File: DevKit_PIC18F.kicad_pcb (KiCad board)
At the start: 2 copper layers, 25 parts, among them J1 PIC_ICSP_ICD, J2 USB_B, J4 RA_PORT, J5 RB_PORT, J6 RD_PORT, J7 RC_PORT, J8 RE_PORT, J9 2P_UART, SW1 SW_DIP, X1 16MHz

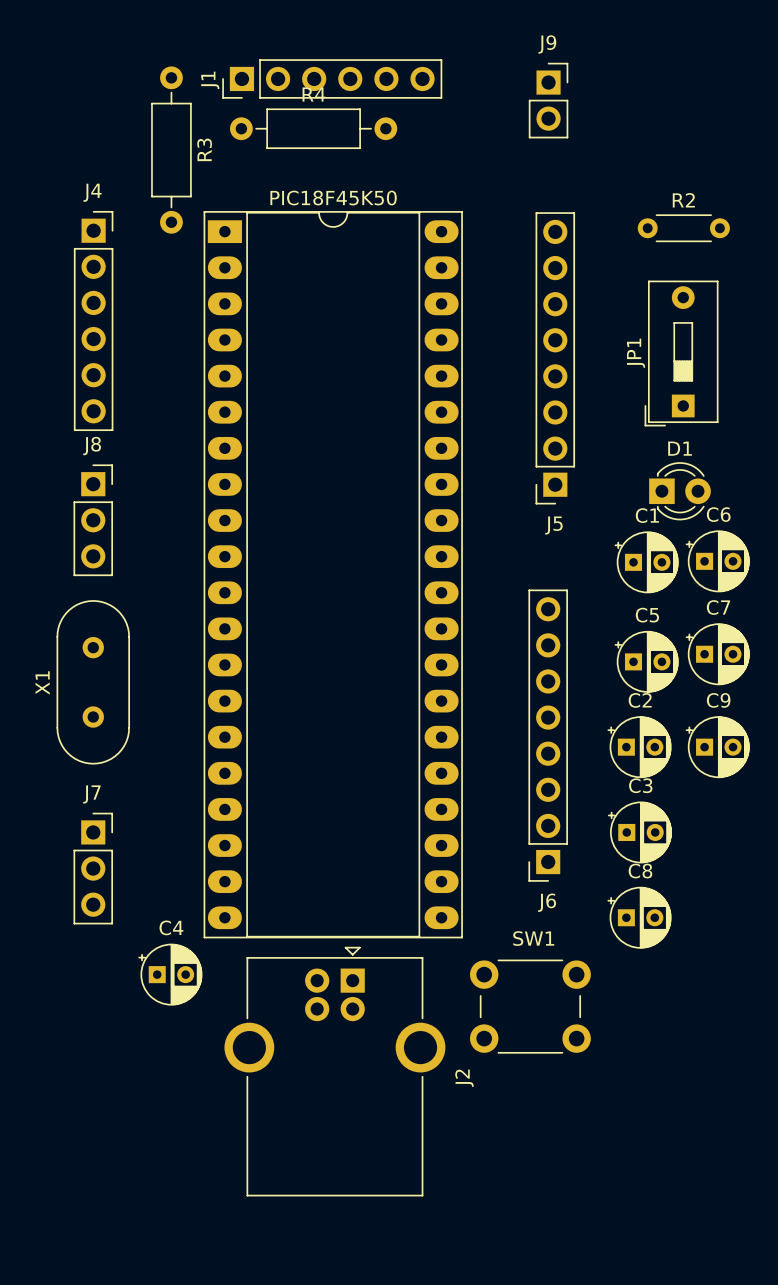
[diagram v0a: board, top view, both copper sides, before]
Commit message: Change USB-B -> USB-C & Added EdgeCut.
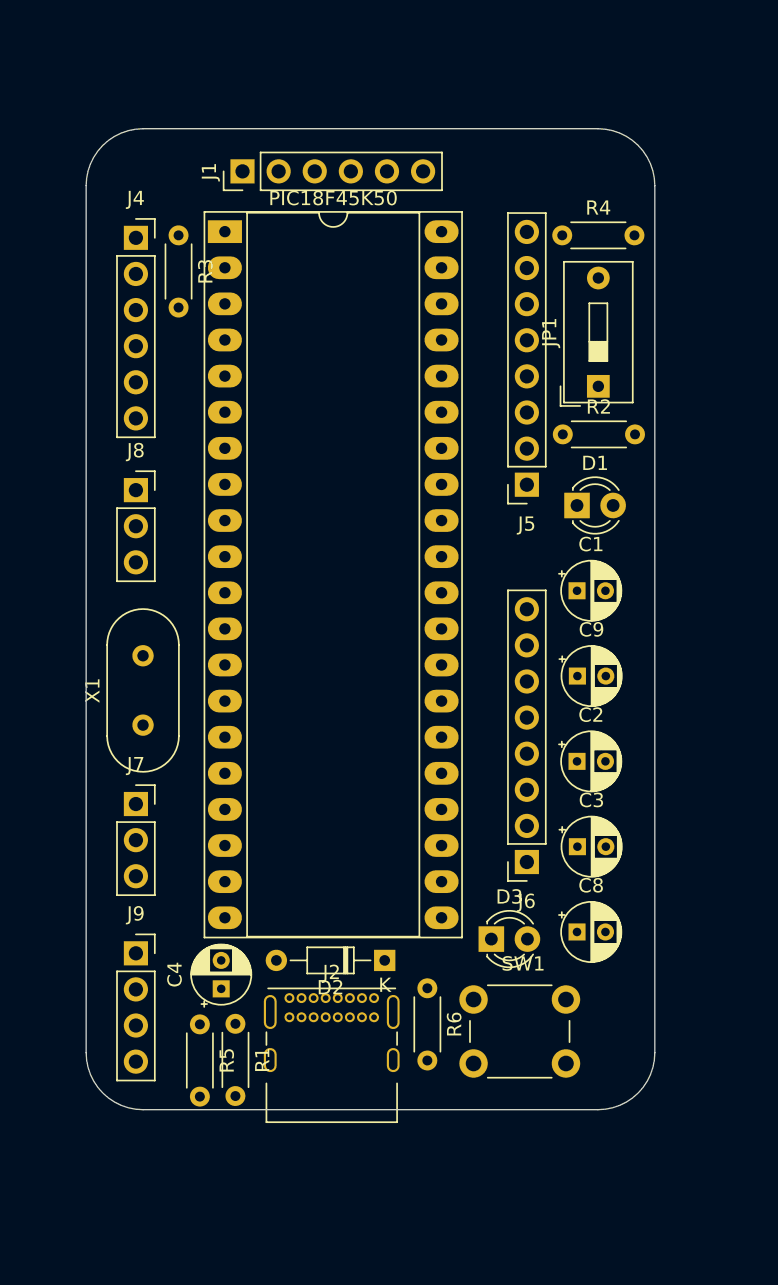
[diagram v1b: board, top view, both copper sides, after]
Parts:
- removed C5: 100nF, Capacitor_THT:CP_Radial_D4.0mm_P2.00mm
- removed C6, C7: 47uF, Capacitor_THT:CP_Radial_D4.0mm_P2.00mm
- added D2: D_Schottky, Diode_THT:D_DO-34_SOD68_P7.62mm_Horizontal, F.Cu at (89.0, 85.0)
- added D3: LED_PWR, LED_THT:LED_D3.0mm_FlatTop, F.Cu at (96.5, 83.5)
- added R1: 5.1k, Resistor_THT:R_Axial_DIN0204_L3.6mm_D1.6mm_P5.08mm_Horizontal, F.Cu at (78.5, 89.5)
- added R5: 5.1k, Resistor_THT:R_Axial_DIN0204_L3.6mm_D1.6mm_P5.08mm_Horizontal, F.Cu at (76.0, 89.5)
- added R6: 330, Resistor_THT:R_Axial_DIN0204_L3.6mm_D1.6mm_P5.08mm_Horizontal, F.Cu at (92.0, 87.0)
- D1: value LED -> LED_RST; footprint LED_THT:LED_D3.0mm -> LED_THT:LED_D3.0mm_FlatTop
- J2: value USB_B -> USB_C_Receptacle_USB2.0_16P; footprint Connector_USB:USB_B_OST_USB-B1HSxx_Horizontal -> Connector_USB:USB_C_Receptacle_GCT_USB4085
- J9: footprint Connector_PinSocket_2.54mm:PinSocket_1x02_P2.54mm_Vertical -> Connector_PinSocket_2.54mm:PinSocket_1x04_P2.54mm_Vertical
- R3, R4: footprint Resistor_THT:R_Axial_DIN0207_L6.3mm_D2.5mm_P10.16mm_Horizontal -> Resistor_THT:R_Axial_DIN0204_L3.6mm_D1.6mm_P5.08mm_Horizontal
- moved J9 67.8 mm to (71.5, 84.5)
- moved R4 23.8 mm to (101.5, 34.0)
- moved R2 15.7 mm to (101.5, 48.0)
- moved R3 11.1 mm to (74.5, 34.0)
- moved C9 10.2 mm to (102.6, 65.0)
- moved J1 6.50 mm to (79.0, 29.5)
- moved JP1 6.13 mm to (104.0, 44.6)
- moved D1 6.06 mm to (102.5, 53.0)
- moved J2 4.62 mm to (82.3, 87.7), turned to 0 degrees
- moved C4 4.61 mm to (77.5, 87.0), turned to 90 degrees
- moved C1 4.45 mm to (102.5, 59.0)
- moved C2 3.61 mm to (102.5, 71.0)
- moved C3 3.61 mm to (102.6, 77.0)
- moved C8 3.61 mm to (102.5, 83.0)
- moved J7 3.61 mm to (71.5, 74.0)
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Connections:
- C1 pad 2: VCC -> GND
- C3 pad 1: VCC -> GND
- C8 pad 1: VCC -> GND
- D1 pad 2: VCC -> GND
- J1 pad 2: VCC -> GND
- JP1 pad 2: VCC -> GND
- PIC18F45K50 pad 1: VCC -> GND
- PIC18F45K50 pad 11: VCC -> GND
- PIC18F45K50 pad 32: VCC -> GND
- R2 pad 2: VCC -> GND
- R3 pad 1: VCC -> GND
- R3 pad 2: VCC -> GND
- R4 pad 2: VCC -> GND
- SW1 pad 1: VCC -> GND
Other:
- board outline added: 40 x 69 mm

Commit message: Routed & Finished Rev.1
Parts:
- J9: footprint Connector_PinSocket_2.54mm:PinSocket_1x04_P2.54mm_Vertical -> Connector_PinSocket_2.54mm:PinSocket_1x05_P2.54mm_Vertical
- moved R3 31.5 mm to (102.0, 49.5), turned to 0 degrees
- moved J6 19.2 mm to (96.5, 59.0), turned to 0 degrees
- moved R5 18.5 mm to (94.5, 89.5)
- moved J5 17.7 mm to (96.5, 34.0), turned to 0 degrees
- moved JP1 15.4 mm to (105.0, 60.0)
- moved R4 13.0 mm to (102.0, 47.0)
- moved D1 11.0 mm to (103.2, 64.0)
- moved C1 10.0 mm to (103.0, 69.0)
- moved C9 9.01 mm to (103.0, 74.0)
- moved C2 8.02 mm to (103.0, 79.0)
- moved C3 7.02 mm to (103.0, 84.0)
- moved R2 6.53 mm to (107.0, 44.5), turned to 180 degrees
- moved D3 4.75 mm to (92.5, 86.0)
- moved C8 4.64 mm to (98.0, 84.0)
- moved J9 3.91 mm to (74.0, 81.5)
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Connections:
- J5 pad 7: /PGD -> /PGC
- J5 pad 8: /PGC -> /PGD
- J9 pad 4: GND -> unconnected-(J9-Pin_4-Pad4)
- PIC18F45K50 pad 39: /PGD -> /PGC
- PIC18F45K50 pad 40: /PGC -> /PGD
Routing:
- net GND: track 0.00 -> 220.5 mm, vias 0 -> 1
- net /PGD: track 0.00 -> 37.2 mm
- net /OSC2: track 0.00 -> 37.0 mm
- net Net-(J6-Pin_1): track 0.00 -> 33.5 mm
- net /MCLR: track 0.00 -> 33.5 mm
- net /OSC1: track 0.00 -> 33.1 mm
- net Net-(J6-Pin_3): track 0.00 -> 31.0 mm, vias 0 -> 3
- net Net-(J6-Pin_2): track 0.00 -> 29.2 mm
- net Net-(J9-Pin_1): track 0.00 -> 27.8 mm
- net Net-(J6-Pin_8): track 0.00 -> 26.2 mm
- net Net-(J6-Pin_7): track 0.00 -> 24.6 mm
- net Net-(J5-Pin_2): track 0.00 -> 24.3 mm
- net Net-(J9-Pin_2): track 0.00 -> 24.1 mm
- net /PGC: track 0.00 -> 22.8 mm
- net Net-(J5-Pin_1): track 0.00 -> 22.1 mm
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- added copper zone on B.Cu, net (none)
- added copper zone on F.Cu, net (none)
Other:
- board size 40 x 69 mm -> 41 x 71 mm
- board text added: "CTS"
- board text added: "GND"
- board text added: "ICSP"
- board text added: "PROG"
- board text added: "RA0"
- board text added: "RA1"
- board text added: "RA2"
- board text added: "RA3"
- board text added: "RA4"
- board text added: "RA5"
- board text added: "RB0/SDI/A"
- board text added: "RB1/SCK/L"
- board text added: "RB2"
- board text added: "RB3/SDO"
- board text added: "RB4"
- board text added: "RB5"
- board text added: "RB6"
- board text added: "RB7"
- board text added: "RC0"
- board text added: "RC1"
- board text added: "RC2"
- board text added: "RD0"
- board text added: "RD1"
- board text added: "RD2"
- board text added: "RD3"
- board text added: "RD4"
- board text added: "RD5"
- board text added: "RD6"
- board text added: "RD7"
- board text added: "RE0"
- board text added: "RE1"
- board text added: "RE2"
- board text added: "RESET"
- board text added: "RX"
- board text added: "TX"
- board text added: "UART"
- board text added: "VCC"

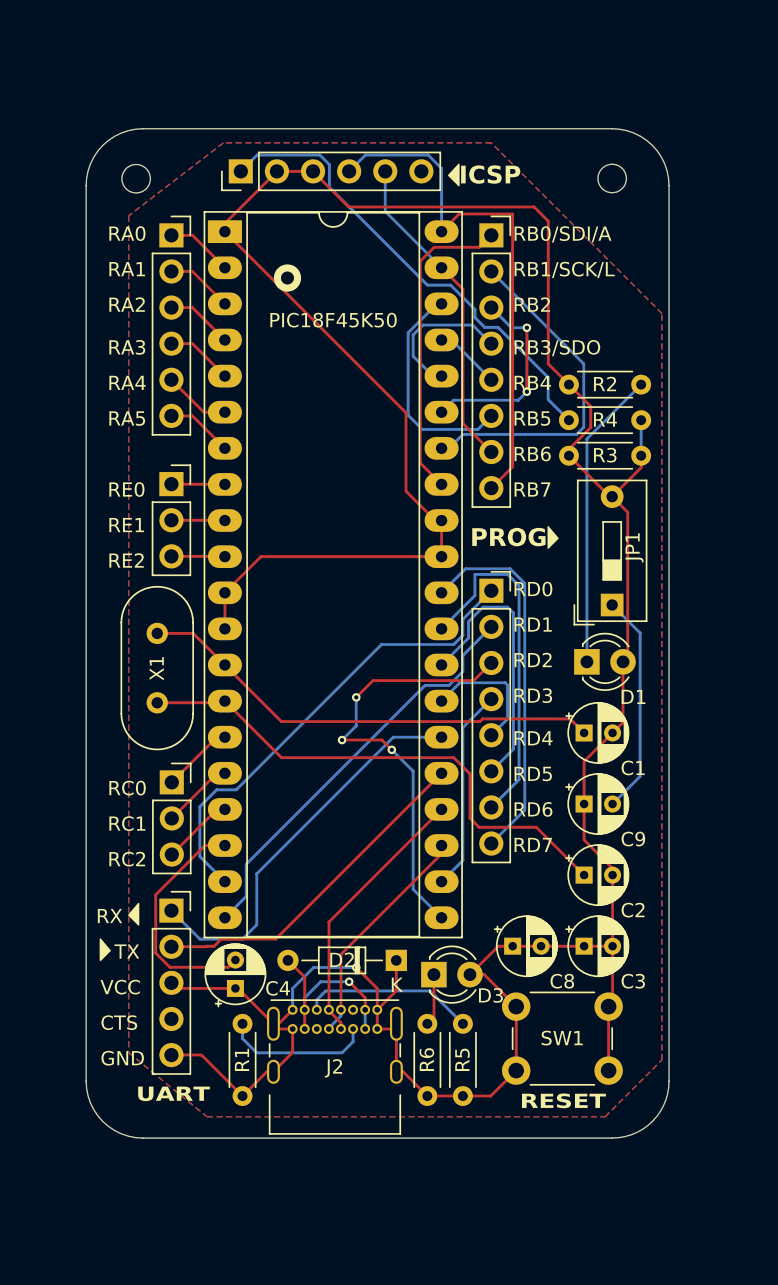
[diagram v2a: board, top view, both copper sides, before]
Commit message: Fixed Crystal Error & re-routed some more.
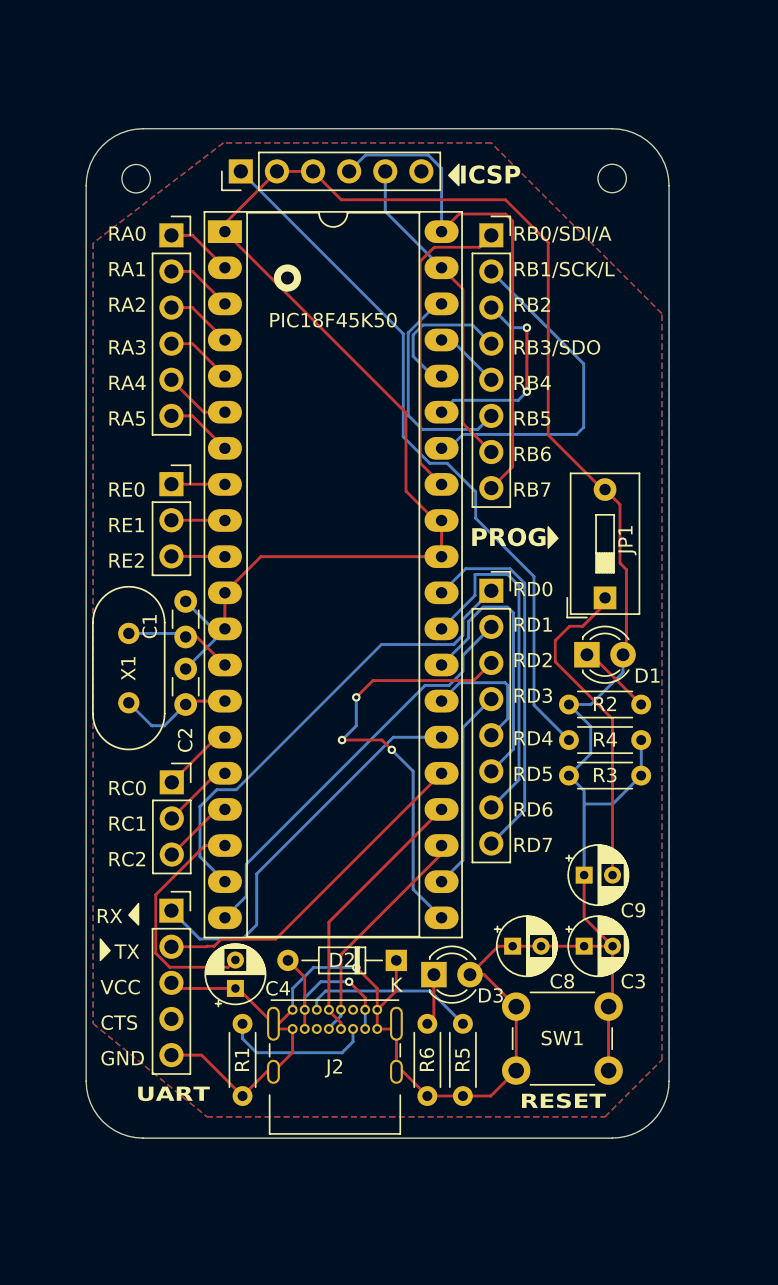
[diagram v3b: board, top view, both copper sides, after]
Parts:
- C1, C2: footprint Capacitor_THT:CP_Radial_D4.0mm_P2.00mm -> Capacitor_THT:C_Disc_D3.0mm_W1.6mm_P2.50mm
- moved C2 30.5 mm to (75.0, 67.0), turned to 90 degrees
- moved C1 28.8 mm to (75.0, 62.2), turned to 90 degrees
- moved R2 22.5 mm to (107.0, 67.0)
- moved R3 22.5 mm to (102.0, 72.0)
- moved R4 22.5 mm to (102.0, 69.5)
- moved C9 5.00 mm to (103.0, 79.0)
- moved X1 2.00 mm to (71.0, 66.9)
- moved JP1 0.71 mm to (104.5, 59.5)
- moved D1 0.50 mm to (103.2, 63.5)
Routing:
- net /OSC2: track 37.0 -> 8.32 mm
- net /OSC1: track 33.1 -> 7.68 mm
- net /MCLR: track 33.5 -> 50.3 mm
- net Net-(D1-K): track 21.1 -> 5.26 mm
- net GND: track 220.5 -> 230.6 mm
- net Net-(JP1-A): track 15.6 -> 23.2 mm

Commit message: refine routing
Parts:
- moved JP1 8.00 mm to (104.5, 67.5)
- moved D1 7.23 mm to (103.2, 56.3)
- moved R2 3.50 mm to (107.0, 70.5)
- moved R3 3.50 mm to (102.0, 75.5)
- moved R4 3.50 mm to (102.0, 73.0)
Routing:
- net Net-(JP1-A): track 23.2 -> 11.7 mm
- net Net-(D1-K): track 5.26 -> 15.8 mm
- net Net-(J6-Pin_3): track 31.0 -> 24.5 mm, vias 3 -> 1
- net Net-(J5-Pin_2): track 24.3 -> 18.0 mm
- net /MCLR: track 50.3 -> 54.6 mm
- net Net-(J6-Pin_1): track 33.5 -> 35.8 mm
- net Net-(J5-Pin_6): track 15.6 -> 17.8 mm
- net Net-(J5-Pin_3): track 14.2 -> 12.3 mm, vias 2 -> 0
- net /PGC: track 22.8 -> 24.1 mm
- net Net-(J6-Pin_8): track 26.2 -> 27.5 mm
- net /OSC2: track 8.32 -> 7.08 mm
- net Net-(J6-Pin_7): track 24.6 -> 25.7 mm
- net /PGD: track 36.9 -> 37.9 mm
- net Net-(PIC18F45K50-VUSB3V3): track 16.6 -> 17.2 mm
- net Net-(J5-Pin_1): track 22.1 -> 22.7 mm

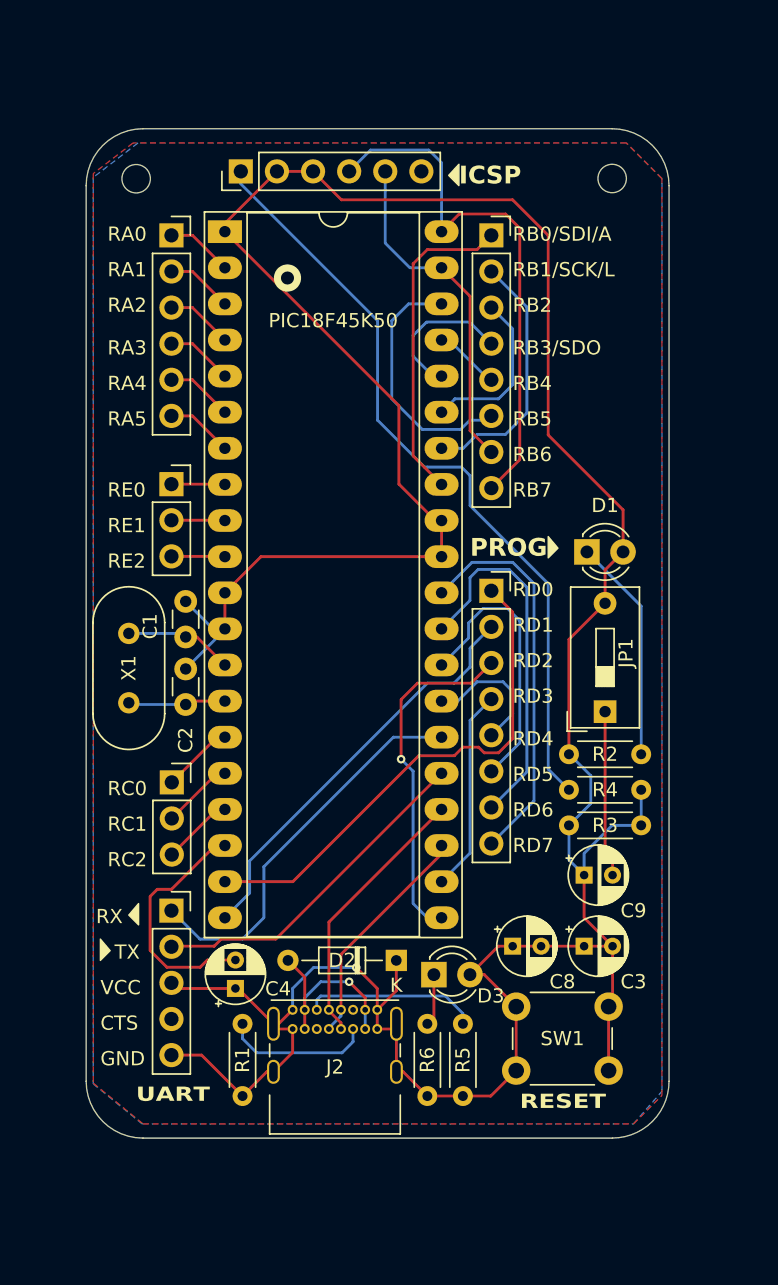
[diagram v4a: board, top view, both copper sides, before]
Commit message: Added ICSP LED, D+/- tuned length, Cap placement/footprint update.
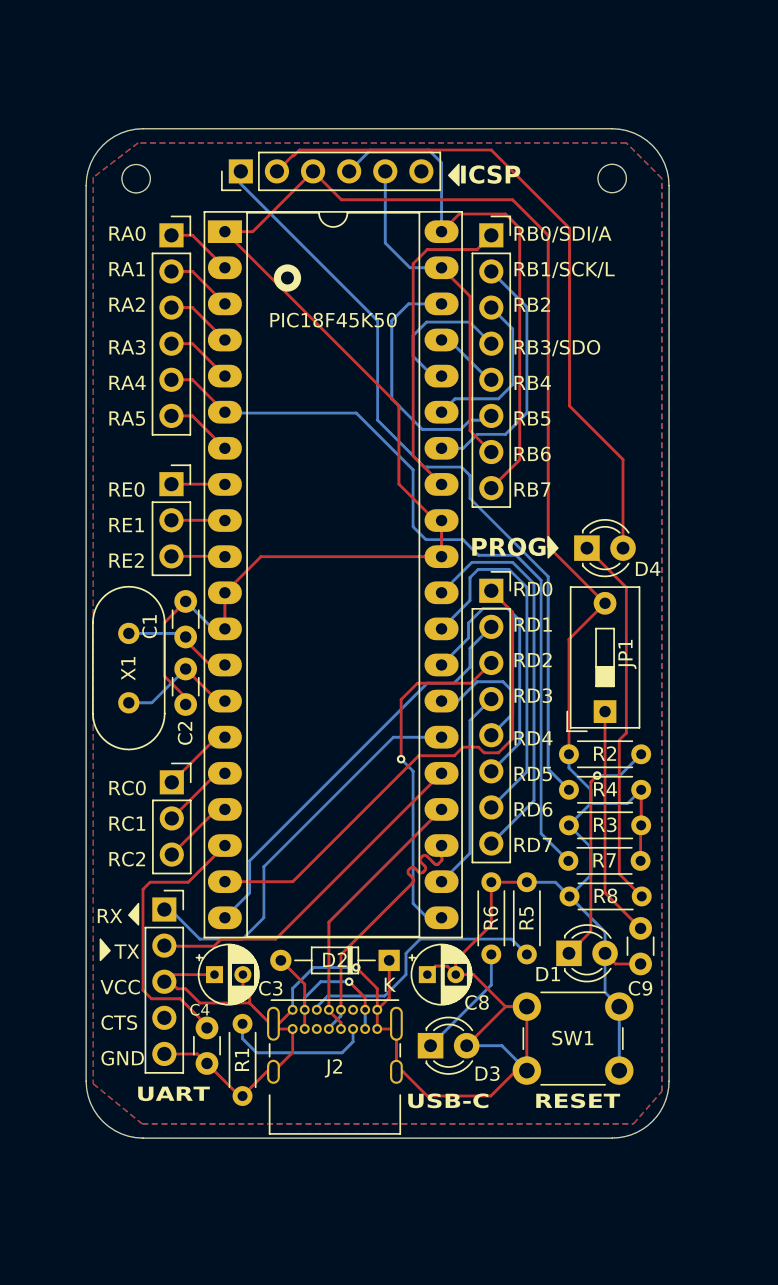
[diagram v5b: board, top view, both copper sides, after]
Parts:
- added D4: LED_VDD, LED_THT:LED_D3.0mm_FlatTop, F.Cu at (103.2, 56.0)
- added R7: 10k, Resistor_THT:R_Axial_DIN0204_L3.6mm_D1.6mm_P5.08mm_Horizontal, F.Cu at (107.0, 78.0)
- added R8: 330, Resistor_THT:R_Axial_DIN0204_L3.6mm_D1.6mm_P5.08mm_Horizontal, F.Cu at (102.0, 80.5)
- C4, C9: footprint Capacitor_THT:CP_Radial_D4.0mm_P2.00mm -> Capacitor_THT:C_Disc_D3.0mm_W1.6mm_P2.50mm
- moved D1 28.3 mm to (102.0, 84.5)
- moved C3 26.1 mm to (77.0, 86.0)
- moved C9 7.41 mm to (107.0, 85.2), turned to 90 degrees
- moved R5 6.64 mm to (99.0, 84.6), turned to 90 degrees
- moved R6 6.64 mm to (96.5, 84.6), turned to 90 degrees
- moved C8 6.32 mm to (92.0, 86.0)
- moved C4 5.64 mm to (76.5, 92.2)
- moved D3 5.01 mm to (92.2, 91.0)
- moved C2 2.50 mm to (75.0, 64.5), turned to -90 degrees
- moved SW1 0.75 mm to (99.0, 88.2)
- moved J9 0.51 mm to (73.5, 81.4)
- moved D2 0.50 mm to (89.3, 85.0)
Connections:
- J1 pad 2: GND -> Net-(D4-A)
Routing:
- net Net-(J4-Pin_5): track 4.70 -> 54.8 mm
- net Net-(D4-A): track 0.00 -> 47.5 mm
- net GND: track 231.1 -> 263.2 mm
- net Net-(D4-K): track 0.00 -> 26.5 mm
- net Net-(J2-CC1): track 12.3 -> 18.3 mm
- net Net-(JP1-A): track 11.7 -> 16.3 mm
- net Net-(D3-K): track 3.65 -> 8.19 mm
- net Net-(PIC18F45K50-VUSB3V3): track 17.2 -> 20.6 mm
- net /D-: track 16.2 -> 19.2 mm
- net /OSC2: track 7.08 -> 8.67 mm
- net Net-(D1-K): track 15.8 -> 17.0 mm, vias 0 -> 1
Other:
- board text added: "DevKit PIC18F45XX Rev.1 : 23th Sep, 2024 Designed by @deulamco"
- board text added: "KiCAD"
- board text added: "Made with"
- board text added: "USB-C"
